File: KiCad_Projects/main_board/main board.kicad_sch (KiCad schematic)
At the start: 77 parts, among them J1 Conn_01x04_Female, J2 Conn_01x04_Female, J3 Conn_01x02_Female, J4 Conn_01x05_Female, SW1 SW_Push, SW2 SW_Push, U1 open_mv, U10 Seeeduino_Xiao, U11 Seeeduino_Xiao, U12 TSSP58038, U13 TSSP58038, U14 TSSP58038, U15 TSSP58038, U2 type-c_sirial, U3 PIC18F26K20_ISS, U4 Akizuki_Logiv_Level_converter, U5 MPU6050, U6 TSSP58038, U7 TSSP58038, U8 TSSP58038, U9 TSSP58038

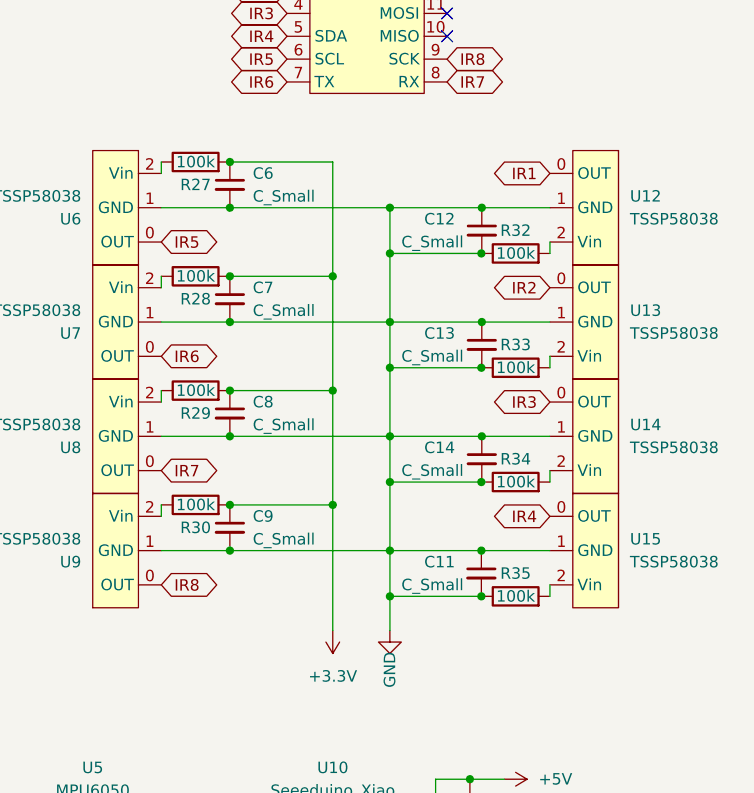
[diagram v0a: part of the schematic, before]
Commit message: 基板データの更新
メイン基板の部品配置まででけた
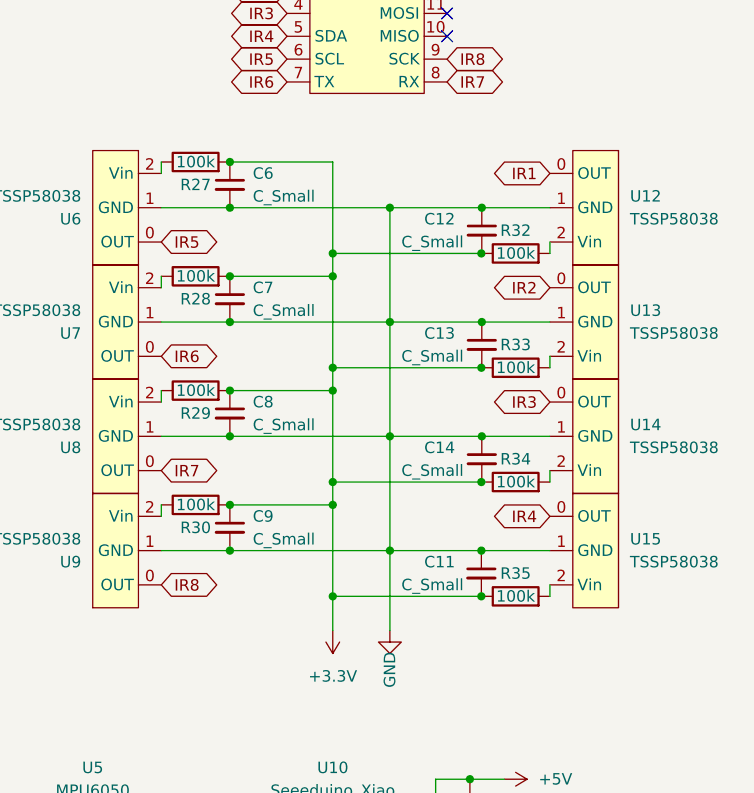
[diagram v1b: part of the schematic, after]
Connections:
- net +3V3: now also C11.2, C12.2, C13.2, C14.2, R32.1, R33.1, R34.1, R35.1
- net GND: no longer C11.2, C12.2, C13.2, C14.2, R32.1, R33.1, R34.1, R35.1
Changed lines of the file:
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@@
   (junction (at 255.27 91.44) (diameter 0) (color 0 0 0 0)
   )
-  (junction (at 245.11 91.44) (diameter 0) (color 0 0 0 0)
-  )
   (junction (at 238.76 93.98) (diameter 0) (color 0 0 0 0)
   )
@@
   (junction (at 255.27 66.04) (diameter 0) (color 0 0 0 0)
   )
+  (junction (at 238.76 78.74) (diameter 0) (color 0 0 0 0)
+  )
   (junction (at 105.41 74.93) (diameter 0) (color 0 0 0 0)
   )
@@
   (junction (at 245.11 60.96) (diameter 0) (color 0 0 0 0)
   )
+  (junction (at 238.76 66.04) (diameter 0) (color 0 0 0 0)
+  )
   (junction (at 71.12 55.88) (diameter 0) (color 0 0 0 0)
   )
@@
   (junction (at 257.81 34.29) (diameter 0) (color 0 0 0 0)
   )
-  (junction (at 245.11 66.04) (diameter 0) (color 0 0 0 0)
-  )
   (junction (at 105.41 99.06) (diameter 0) (color 0 0 0 0)
   )
@@
   (junction (at 254 132.08) (diameter 0) (color 0 0 0 0)
   )
-  (junction (at 245.11 78.74) (diameter 0) (color 0 0 0 0)
-  )
   (junction (at 238.76 81.28) (diameter 0) (color 0 0 0 0)
   )
@@
   (junction (at 227.33 73.66) (diameter 0) (color 0 0 0 0)
   )
-  (junction (at 245.11 104.14) (diameter 0) (color 0 0 0 0)
+  (junction (at 238.76 104.14) (diameter 0) (color 0 0 0 0)
   )
   (junction (at 261.62 149.86) (diameter 0) (color 0 0 0 0)
@@
   )
   (junction (at 175.26 74.93) (diameter 0) (color 0 0 0 0)
+  )
+  (junction (at 238.76 91.44) (diameter 0) (color 0 0 0 0)
   )
   (junction (at 162.56 109.22) (diameter 0) (color 0 0 0 0)
@@
   (no_connect (at 251.46 41.91))
   (no_connect (at 251.46 39.37))
-  (wire (pts (xy 245.11 99.06) (xy 245.11 104.14))
+  (wire (pts (xy 238.76 66.04) (xy 238.76 68.58))
     (stroke (width 0) (type default) (color 0 0 0 0))
   )
@@
     (stroke (width 0) (type default) (color 0 0 0 0))
   )
-  (wire (pts (xy 245.11 60.96) (xy 245.11 66.04))
-    (stroke (width 0) (type default) (color 0 0 0 0))
-  )
   (wire (pts (xy 245.11 86.36) (xy 255.323 86.36))
     (stroke (width 0) (type default) (color 0 0 0 0))
@@
     (stroke (width 0) (type default) (color 0 0 0 0))
   )
-  (wire (pts (xy 245.11 91.44) (xy 245.11 99.06))
+  (wire (pts (xy 245.11 86.36) (xy 245.11 99.06))
     (stroke (width 0) (type default) (color 0 0 0 0))
   )
@@
     (stroke (width 0) (type default) (color 0 0 0 0))
   )
+  (wire (pts (xy 238.76 91.44) (xy 238.76 93.98))
+    (stroke (width 0) (type default) (color 0 0 0 0))
+  )
   (wire (pts (xy 162.56 74.93) (xy 165.1 74.93))
     (stroke (width 0) (type default) (color 0 0 0 0))
@@
     (stroke (width 0) (type default) (color 0 0 0 0))
   )
+  (wire (pts (xy 245.11 60.96) (xy 245.11 73.66))
+    (stroke (width 0) (type default) (color 0 0 0 0))
+  )
   (wire (pts (xy 255.27 78.74) (xy 255.323 78.74))
     (stroke (width 0) (type default) (color 0 0 0 0))
@@
     (stroke (width 0) (type default) (color 0 0 0 0))
   )
-  (wire (pts (xy 238.76 55.88) (xy 238.76 68.58))
+  (wire (pts (xy 238.76 55.88) (xy 238.76 66.04))
     (stroke (width 0) (type default) (color 0 0 0 0))
   )
@@
     (stroke (width 0) (type default) (color 0 0 0 0))
   )
-  (wire (pts (xy 245.11 86.36) (xy 245.11 91.44))
-    (stroke (width 0) (type default) (color 0 0 0 0))
-  )
   (wire (pts (xy 44.45 142.24) (xy 57.15 142.24))
     (stroke (width 0) (type default) (color 0 0 0 0))
@@
     (stroke (width 0) (type default) (color 0 0 0 0))
   )
-  (wire (pts (xy 255.27 91.44) (xy 245.11 91.44))
-    (stroke (width 0) (type default) (color 0 0 0 0))
-  )
   (wire (pts (xy 71.12 60.96) (xy 71.12 76.2))
     (stroke (width 0) (type default) (color 0 0 0 0))
@@
     (stroke (width 0) (type default) (color 0 0 0 0))
   )
-  (wire (pts (xy 238.76 68.58) (xy 238.76 81.28))
+  (wire (pts (xy 238.76 68.58) (xy 238.76 78.74))
     (stroke (width 0) (type default) (color 0 0 0 0))
   )
@@
     (stroke (width 0) (type default) (color 0 0 0 0))
   )
-  (wire (pts (xy 238.76 81.28) (xy 238.76 93.98))
+  (wire (pts (xy 238.76 81.28) (xy 238.76 91.44))
     (stroke (width 0) (type default) (color 0 0 0 0))
   )
@@
     (stroke (width 0) (type default) (color 0 0 0 0))
   )
+  (wire (pts (xy 238.76 78.74) (xy 238.76 81.28))
+    (stroke (width 0) (type default) (color 0 0 0 0))
+  )
   (wire (pts (xy 165.1 74.93) (xy 167.64 74.93))
     (stroke (width 0) (type default) (color 0 0 0 0))
@@
     (stroke (width 0) (type default) (color 0 0 0 0))
   )
-  (wire (pts (xy 255.27 66.04) (xy 245.11 66.04))
+  (wire (pts (xy 238.76 66.04) (xy 255.27 66.04))
     (stroke (width 0) (type default) (color 0 0 0 0))
   )
@@
     (stroke (width 0) (type default) (color 0 0 0 0))
   )
-  (wire (pts (xy 245.11 66.04) (xy 245.11 73.66))
+  (wire (pts (xy 238.76 91.44) (xy 255.27 91.44))
     (stroke (width 0) (type default) (color 0 0 0 0))
   )
@@
     (stroke (width 0) (type default) (color 0 0 0 0))
   )
-  (wire (pts (xy 255.27 78.74) (xy 245.11 78.74))
+  (wire (pts (xy 238.76 78.74) (xy 255.27 78.74))
     (stroke (width 0) (type default) (color 0 0 0 0))
   )
@@
     (stroke (width 0) (type default) (color 0 0 0 0))
   )
-  (wire (pts (xy 238.76 93.98) (xy 238.76 107.95))
+  (wire (pts (xy 238.76 93.98) (xy 238.76 104.14))
     (stroke (width 0) (type default) (color 0 0 0 0))
   )
@@
     (stroke (width 0) (type default) (color 0 0 0 0))
   )
-  (wire (pts (xy 255.27 104.14) (xy 245.11 104.14))
-    (stroke (width 0) (type default) (color 0 0 0 0))
-  )
   (wire (pts (xy 254 26.67) (xy 257.81 26.67))
     (stroke (width 0) (type default) (color 0 0 0 0))
@@
     (stroke (width 0) (type default) (color 0 0 0 0))
   )
-  (wire (pts (xy 245.11 78.74) (xy 245.11 86.36))
+  (wire (pts (xy 245.11 73.66) (xy 245.11 86.36))
     (stroke (width 0) (type default) (color 0 0 0 0))
   )
@@
     (stroke (width 0) (type default) (color 0 0 0 0))
   )
+  (wire (pts (xy 238.76 104.14) (xy 238.76 107.95))
+    (stroke (width 0) (type default) (color 0 0 0 0))
+  )
   (wire (pts (xy 219.71 60.96) (xy 227.33 60.96))
     (stroke (width 0) (type default) (color 0 0 0 0))
@@
     (stroke (width 0) (type default) (color 0 0 0 0))
   )
-  (wire (pts (xy 245.11 104.14) (xy 245.11 107.95))
+  (wire (pts (xy 245.11 99.06) (xy 245.11 107.95))
     (stroke (width 0) (type default) (color 0 0 0 0))
   )
@@
     (stroke (width 0) (type default) (color 0 0 0 0))
   )
-  (wire (pts (xy 245.11 73.66) (xy 245.11 78.74))
-    (stroke (width 0) (type default) (color 0 0 0 0))
-  )
+  (wire (pts (xy 238.76 104.14) (xy 255.27 104.14))
+    (stroke (width 0) (type default) (color 0 0 0 0))
+  )

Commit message: 基板データの更新
最後に更新してからのデータ全てです。
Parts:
- removed C11, C12, C13, C14, C6, C7, C8, C9: C_Small, Capacitor_THT:C_Disc_D3.8mm_W2.6mm_P2.50mm, symbol Device:C_Small
- removed R27, R28, R29, R30, R32, R33, R34, R35: 100k, Resistor_THT:R_Axial_DIN0204_L3.6mm_D1.6mm_P5.08mm_Horizontal, symbol Device:R
- added C? (x8): C_Small, Capacitor_THT:C_Disc_D3.8mm_W2.6mm_P2.50mm, symbol Device:C_Small
- added R? (x8): 100k, Resistor_THT:R_Axial_DIN0204_L3.6mm_D1.6mm_P5.08mm_Horizontal, symbol Device:R
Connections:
- net +3V3: now also U12.2 (Vin), U13.2 (Vin), U14.2 (Vin), U15.2 (Vin), U6.2 (Vin), U7.2 (Vin), U8.2 (Vin), U9.2 (Vin)
- net GND: now also C?.1, C?.1, C?.1, C?.1, C?.2, C?.2, C?.2, C?.2; no longer U10.2
- net IR1: now also C?.1, R?.1; no longer U12.0 (OUT)
- net IR2: now also C?.1, R?.1; no longer U13.0 (OUT)
- net IR3: now also C?.1, R?.1; no longer U14.0 (OUT)
- net IR4: now also C?.1, R?.1; no longer U15.0 (OUT)
- net IR5: now also C?.2, R?.2; no longer U6.0 (OUT)
- net IR6: now also C?.2, R?.2; no longer U7.0 (OUT)
- net IR7: now also C?.2, R?.2; no longer U8.0 (OUT)
- net IR8: now also C?.2, R?.2; no longer U9.0 (OUT)
- net RES: now reaches C16.1, R31.2, SW2.1
- net RES: now also U10.2
- new net: R?.2, U12.0 (OUT)
- new net: R?.2, U15.0 (OUT)
- new net: R?.2, U13.0 (OUT)
- new net: R?.1, U6.0 (OUT)
- new net: R?.2, U14.0 (OUT)
- new net: R?.1, U8.0 (OUT)
- new net: R?.1, U9.0 (OUT)
- new net: R?.1, U7.0 (OUT)

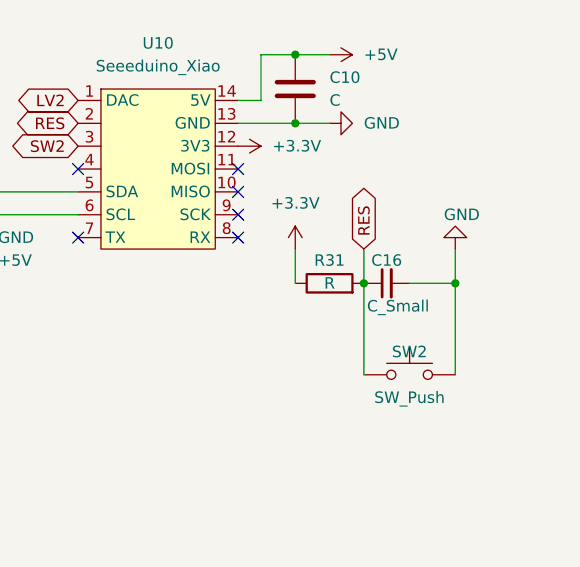
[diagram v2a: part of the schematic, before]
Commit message: 基板データの更新
IO基板のCNCバージョン作成
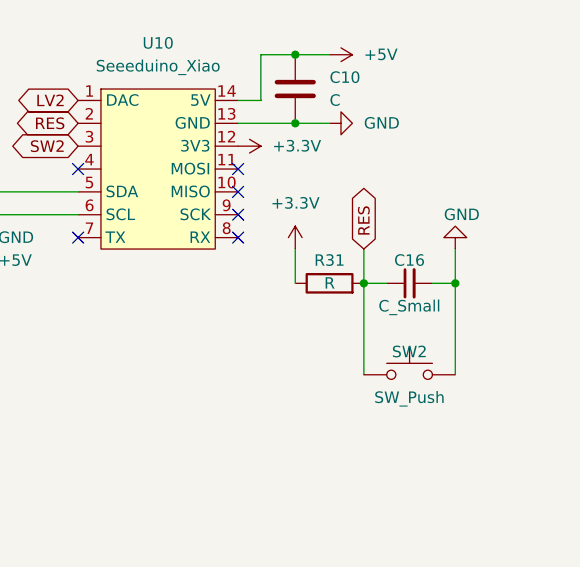
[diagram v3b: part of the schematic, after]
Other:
- moved on the sheet: C16
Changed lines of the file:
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@@
+    (stroke (width 0) (type default) (color 0 0 0 0))
+  )
+  (wire (pts (xy 264.16 149.86) (xy 261.62 149.86))
     (stroke (width 0) (type default) (color 0 0 0 0))
   )
@@
     (stroke (width 0) (type default) (color 0 0 0 0))
   )
-  (wire (pts (xy 266.7 149.86) (xy 271.78 149.86))
+  (wire (pts (xy 269.24 149.86) (xy 271.78 149.86))
     (stroke (width 0) (type default) (color 0 0 0 0))
   )
@@
     (pin "2")
   )
-  (symbol (lib_id "Device:C_Small") (at 264.16 149.86 90) (unit 1)
-    (in_bom yes) (on_board yes)
-    (property "Reference" "C16" (id 0) (at 264.16 147.32 90))
-    (property "Value" "C_Small" (id 1) (at 265.43 152.4 90))
-    (property "Footprint" "Capacitor_THT:C_Disc_D3.8mm_W2.6mm_P2.50mm" (id 2) (at 264.16 149.86 0)
-      (effects (font (size 1.27 1.27)) hide)
-    )
-    (property "Datasheet" "~" (id 3) (at 264.16 149.86 0)
-      (effects (font (size 1.27 1.27)) hide)
-    )
+  (symbol (lib_id "Device:C_Small") (at 266.7 149.86 90) (unit 1)
+    (in_bom yes) (on_board yes)
+    (property "Reference" "C16" (id 0) (at 266.7 147.32 90))
+    (property "Value" "C_Small" (id 1) (at 266.7 152.4 90))
+    (property "Footprint" "Capacitor_THT:C_Disc_D3.8mm_W2.6mm_P2.50mm" (id 2) (at 266.7 149.86 0)
+      (effects (font (size 1.27 1.27)) hide)
+    )
+    (property "Datasheet" "~" (id 3) (at 266.7 149.86 0)
+      (effects (font (size 1.27 1.27)) hide)
+    )
